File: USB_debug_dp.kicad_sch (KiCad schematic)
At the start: 140 parts, among them J3 USB-C_GCT_USB4105-GF-A, J4 USB-C_Amphenol_12401598E4, J9 Tag-Connect_TC2050-IDC-NL_2x5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, Q2 PJE138K, U11 TPD4E05U06QDQARQ1, U13 TUSB1046-DCIRNQ, U15 AP22615A_TSOT26, U17 TPD4E05U06QDQARQ1, U18 TPD4E05U06QDQARQ1, U19 TPD4E05U06QDQARQ1, U20 TPD4E05U06QDQARQ1, U3 NTS0102_XSON, U4 FT230X_QFN, U4 NCP730BMT330_WSON, U5 AP22615A_TSOT26, U6 TPS65988DHRSHR, U8 TPS65988DHRSHR, U9 W25Q80DV_USON

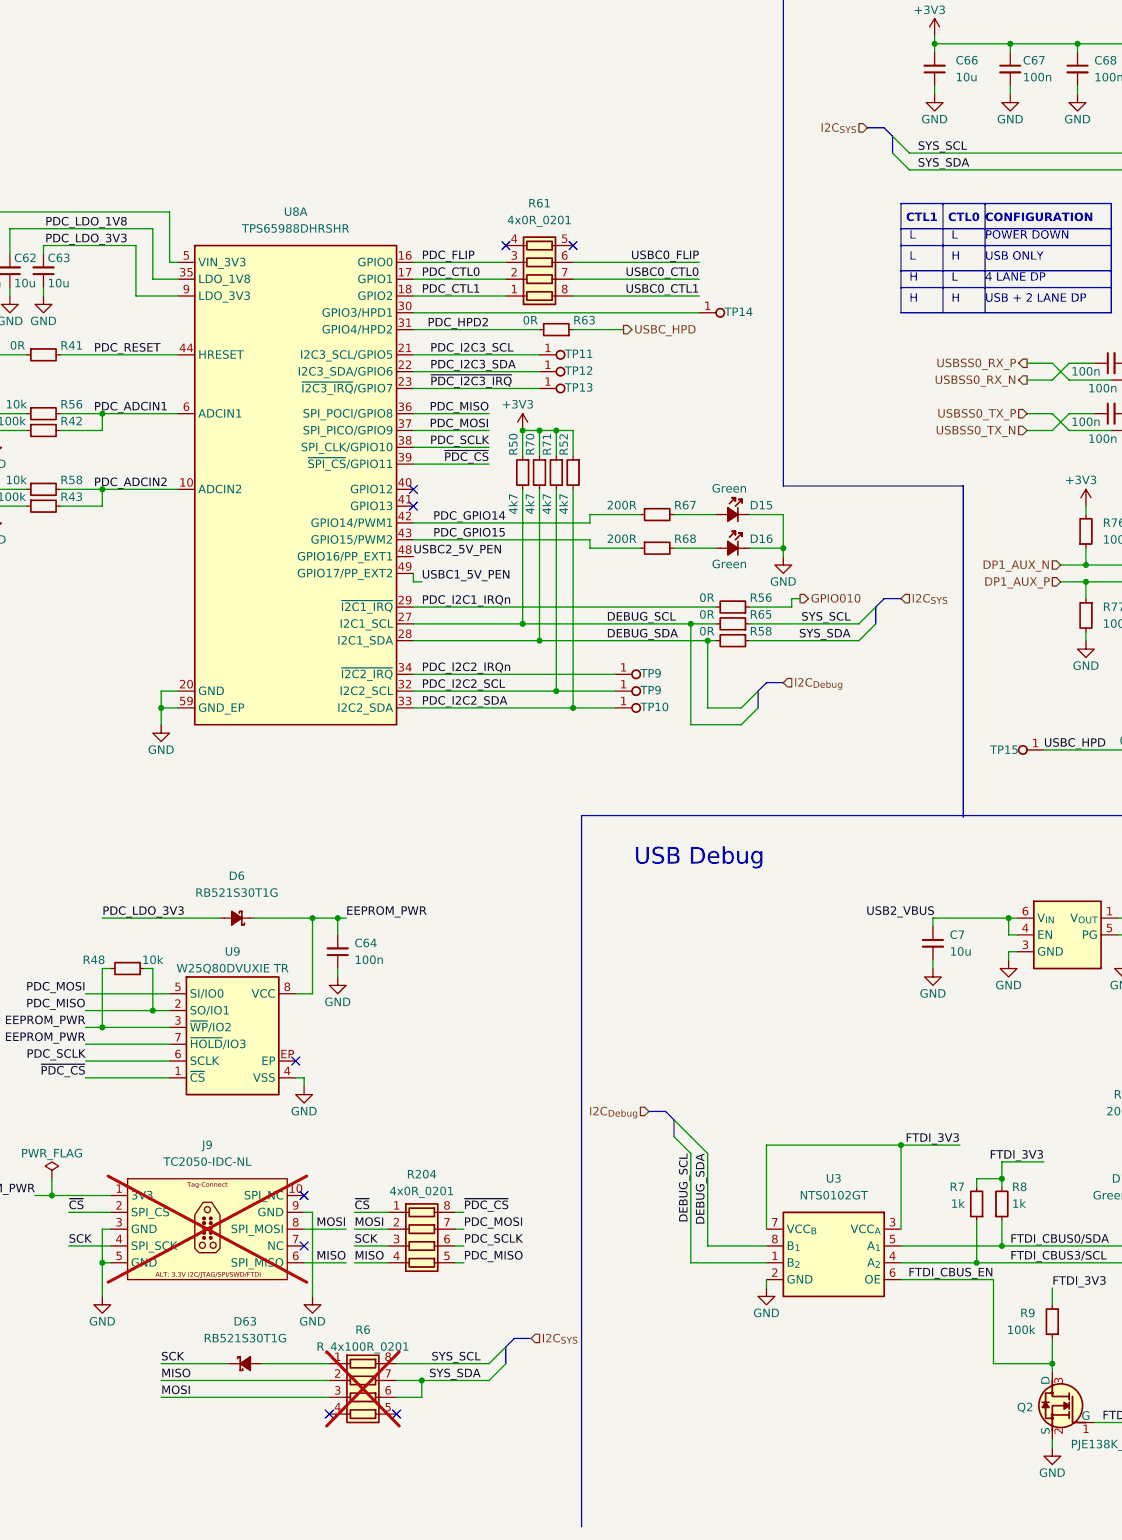
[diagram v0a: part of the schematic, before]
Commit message: [#82055] Add interface controller for USBC0
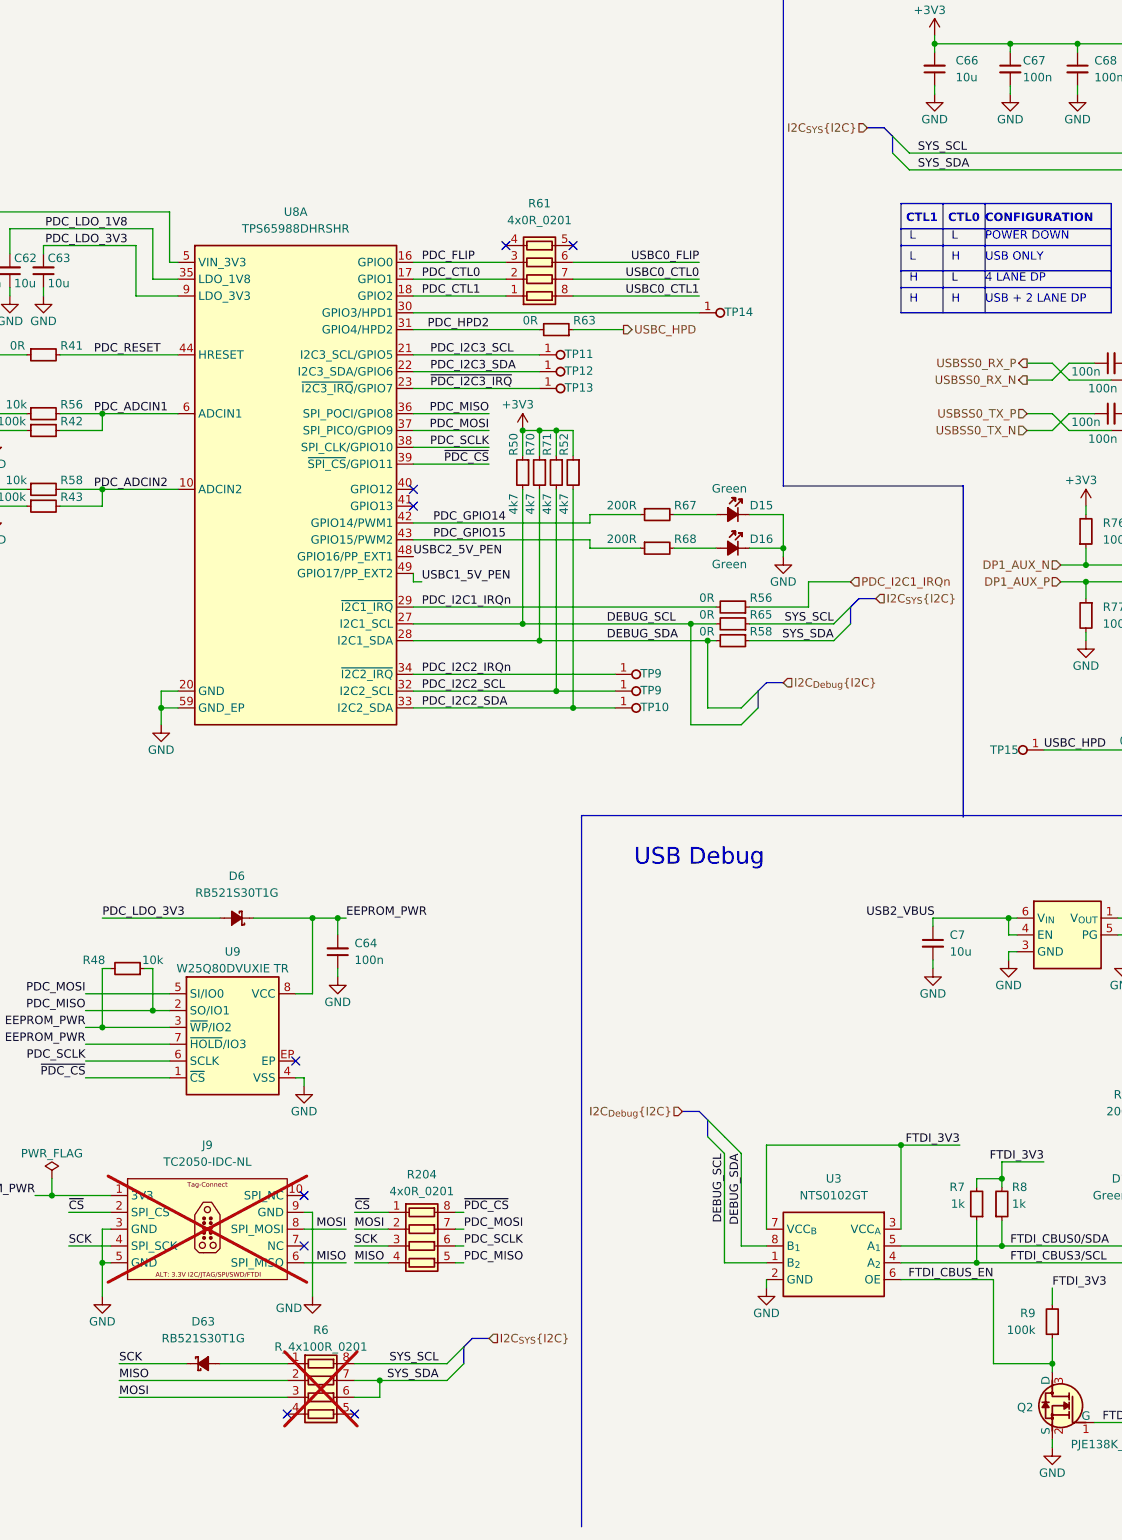
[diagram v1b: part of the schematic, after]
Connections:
- net GPIO010 is gone; now on net PDC_I2C1_IRQn: R56.1
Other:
- moved on the sheet: D63, R6

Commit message: [#82055] Add port 3,4 connect to hub
[#82055] Change I2C bus

[#82055] Cleanup pin assigment

[#82055] Cleanup
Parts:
- added R236: R_4x0R_0201_array, antmicro-footprints:R_Array_4x0201_Panasonic_EXB18V, symbol antmicroResistorNetworksArrays:R_4x0R_0201_array
- renumbered C63 to C100, C64 to C101, C7 to C102, C66 to C103, C67 to C104, C68 to C105, C69 to C106, C70 to C107, C71 to C108, C72 to C109, C73 to C110, C74 to C111, C1 to C112, C2 to C113, C3 to C114, C83 to C115, C40 to C116, C89 to C117, C90 to C118, C7 to C119, C81 to C120, C82 to C121, C53 to C122, C86 to C123, C87 to C124, C136 to C125, C35 to C126, C45 to C127, C8 to C128, C9 to C129, C5 to C130, C6 to C131, C65 to C132, C149 to C133, C60 to C97, C61 to C98, C62 to C99, D63 to D21, D6 to D22, D15 to D23, D16 to D24, D1 to D25, D2 to D26, D7 to D27, D3 to D28, D8 to D29, D9 to D30, J4 to J10, J9 to J8, J3 to J9, Q2 to Q12, R41 to R116, R56 to R117, R42 to R118, R58 to R119, R43 to R120, R48 to R121, R6 to R122, R204 to R123, R61 to R124, R50 to R125, R70 to R126, R71 to R127, R63 to R128, R52 to R129, R67 to R130, R68 to R131, R56 to R132, R65 to R133, R58 to R134, R7 to R135, R8 to R136, R9 to R137, R76 to R138, R77 to R139, R61 to R140, R10 to R141, R11 to R142, R81 to R143, R65 to R144, R12 to R145, R13 to R146, R14 to R147, R15 to R148, R87 to R149, R100 to R150, R101 to R151, R102 to R152, R103 to R153, R104 to R154, R105 to R155, R106 to R156, R107 to R157, R108 to R158, R67 to R159, R68 to R160, R111 to R161, R70 to R162, R113 to R163, R90 to R164, R92 to R165, R94 to R166, R16 to R167, R96 to R168, R17 to R169, R18 to R170, R144 to R171, R74 to R172, R20 to R173, R21 to R174, R78 to R175, R98 to R176, R99 to R177, R19 to R178, R1 to R179, TP11 to TP25, TP12 to TP26, TP13 to TP27, TP9 to TP28, TP9 to TP29, TP10 to TP30, TP14 to TP31, TP15 to TP32, TP16 to TP33, TP27 to TP34, TP17 to TP35, U9 to U23, U8 to U24, U3 to U25, U4 to U26, U13 to U27, U4 to U28, U15 to U29, U20 to U30, U19 to U31, U17 to U32, U6 to U33, U5 to U34, U18 to U35, U11 to U36
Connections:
- net MISO: now also R236.4 (R4.1)
- net MOSI: now also R236.2 (R2.1)
- net SCK: now also R236.3 (R3.1)
- net ~{CS}: now also R236.1 (R1.1)
- net EEPROM_PWR renamed FLASH_PWR
- new net HUB_MISO: R236.5 (R4.2)
- new net HUB_MOSI: R236.7 (R2.2)
- new net HUB_SCLK: R236.6 (R3.2)
- new net ~{HUB_CS}: R236.8 (R1.2)
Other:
- moved on the sheet: D21, J8, R122, R123

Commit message: [#82055] Fix labels
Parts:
- renumbered C97 to C133, C98 to C134, C99 to C135, C100 to C136, C101 to C137, C102 to C138, C103 to C139, C104 to C140, C105 to C141, C106 to C142, C107 to C143, C108 to C144, C109 to C145, C110 to C146, C111 to C147, C112 to C148, C113 to C149, C114 to C150, C115 to C151, C116 to C152, C117 to C153, C118 to C154, C119 to C155, C120 to C156, C121 to C157, C122 to C158, C123 to C159, C124 to C160, C125 to C161, C126 to C162, C127 to C163, C128 to C164, C129 to C165, C130 to C166, C131 to C167, C132 to C168, C133 to C169, D21 to D22, D22 to D23, D23 to D24, D24 to D25, D25 to D26, D26 to D27, D27 to D28, D28 to D29, D29 to D30, D30 to D31, J8 to J10, J9 to J11, J10 to J12, R116 to R136, R117 to R137, R118 to R138, R119 to R139, R120 to R140, R121 to R141, R236 to R142, R122 to R143, R123 to R144, R124 to R145, R125 to R146, R126 to R147, R127 to R148, R128 to R149, R129 to R150, R130 to R151, R131 to R152, R132 to R153, R133 to R154, R134 to R155, R135 to R156, R136 to R157, R137 to R158, R138 to R159, R139 to R160, R140 to R161, R141 to R162, R142 to R163, R143 to R164, R144 to R165, R145 to R166, R146 to R167, R147 to R168, R148 to R169, R149 to R170, R150 to R171, R151 to R172, R152 to R173, R153 to R174, R154 to R175, R155 to R176, R156 to R177, R157 to R178, R158 to R179, R159 to R180, R160 to R181, R161 to R182, R162 to R183, R163 to R184, R164 to R185, R165 to R186, R166 to R187, R167 to R188, R168 to R189, R169 to R190, R170 to R191, R171 to R192, R172 to R193, R173 to R194, R174 to R195, R175 to R196, R176 to R197, R177 to R198, R178 to R199, R179 to R200, U23 to U29, U24 to U30, U25 to U31, U26 to U32, U27 to U33, U28 to U34, U29 to U35, U30 to U36, U31 to U37, U32 to U38, U33 to U39, U34 to U40, U35 to U41, U36 to U42

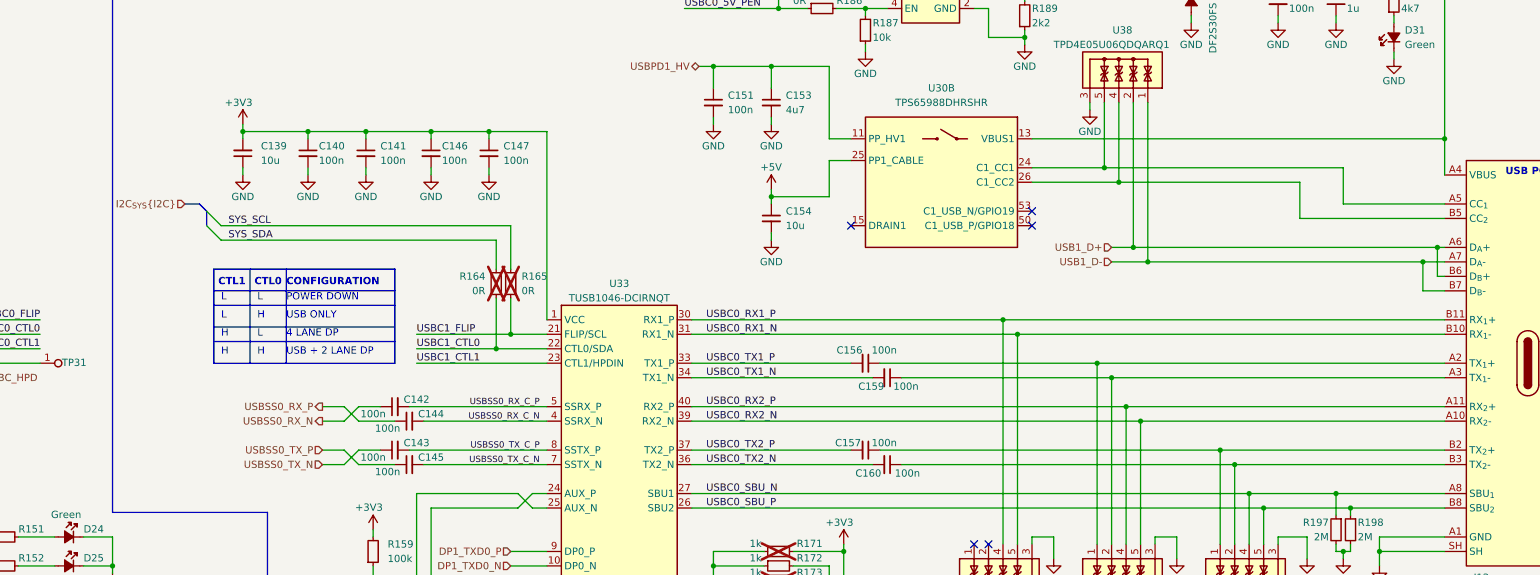
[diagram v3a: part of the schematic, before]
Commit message: [#82055] Add ESD protection
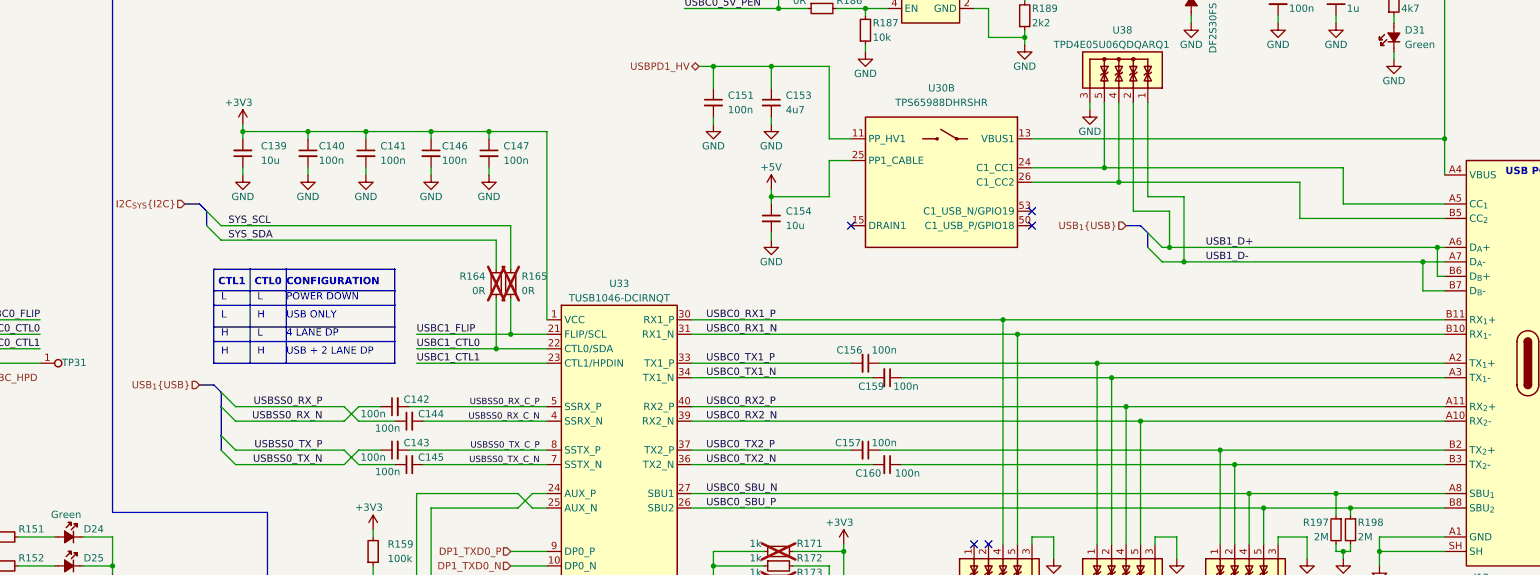
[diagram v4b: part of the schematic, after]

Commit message: [#82757] Rename project to jetson-agx-thor-baseboard
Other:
- title: Jetson Orin AGX Baseboard -> Jetson AGX Thor Baseboard
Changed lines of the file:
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@@
 	(paper "A3")
 	(title_block
-		(title "Jetson Orin AGX Baseboard")
+		(title "Jetson AGX Thor Baseboard")
 		(date "2025-08-11")
 		(rev "1.0.0")

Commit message: [#82757] Cleanup: reorganise page numbers and fix annotations
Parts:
- renumbered C133 to C118, C134 to C119, C135 to C120, C136 to C121, C137 to C122, C138 to C123, C139 to C124, C140 to C125, C141 to C126, C142 to C127, C143 to C128, C144 to C129, C145 to C130, C146 to C131, C147 to C132, C148 to C133, C149 to C134, C150 to C135, C151 to C136, C152 to C137, C153 to C138, C154 to C139, C155 to C140, C156 to C141, C157 to C142, C158 to C143, C159 to C144, C160 to C145, C161 to C146, C162 to C147, C163 to C148, C164 to C149, C165 to C150, C166 to C151, C167 to C152, C168 to C153, C169 to C154, D22 to D16, D23 to D17, D24 to D18, D25 to D19, D26 to D20, D27 to D21, D28 to D22, D29 to D23, D30 to D24, D31 to D25, J10 to J7, J11 to J8, J12 to J9, R143 to R100, R144 to R101, R145 to R102, R146 to R103, R147 to R104, R148 to R105, R149 to R106, R150 to R107, R151 to R108, R152 to R109, R153 to R110, R154 to R111, R155 to R112, R156 to R113, R157 to R114, R158 to R115, R159 to R116, R160 to R117, R161 to R118, R162 to R119, R163 to R120, R164 to R121, R165 to R122, R166 to R123, R167 to R124, R168 to R125, R169 to R126, R170 to R127, R171 to R128, R172 to R129, R173 to R130, R174 to R131, R175 to R132, R176 to R133, R177 to R134, R178 to R135, R179 to R136, R180 to R137, R181 to R138, R182 to R139, R183 to R140, R184 to R141, R185 to R142, R186 to R143, R187 to R144, R188 to R145, R189 to R146, R190 to R147, R191 to R148, R192 to R149, R193 to R150, R194 to R151, R195 to R152, R196 to R153, R197 to R154, R198 to R155, R199 to R156, R200 to R157, R136 to R93, R137 to R94, R138 to R95, R139 to R96, R140 to R97, R141 to R98, R142 to R99, TP25 to TP10, TP26 to TP11, TP27 to TP12, TP28 to TP13, TP29 to TP14, TP30 to TP15, TP31 to TP16, TP32 to TP17, TP33 to TP18, TP34 to TP19, TP35 to TP20
